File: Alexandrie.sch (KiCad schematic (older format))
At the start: 61 parts

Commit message: Angelia lpf/hpf Control board
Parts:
- removed U?: TPIC6B595, symbol TPIC6B595
- removed U?: 74HCT04, symbol 74HCT04
- added C11, C13, C15, C16, C18, C20: 100n, symbol C_Small
- added C12, C14, C17, C19: 10u, symbol CP_Small
- added J5: CONN_01X02, symbol CONN_01X02
- added U11: LD29150DT50R, symbol 7805D-Pack
- added U12: L4940D2T12, symbol 7805D-Pack
- added unit 2 of U2
- added U8: TPIC6B595, symbol TPIC6B595-RESCUE-Alexandrie-RESCUE-Alexandrie
- J1: renamed from J?; value CONN_01X10 -> kk_10
- J2: renamed from J?; value CONN_01X05 -> kk_5
- J3: renamed from J?; value Antenna_Conn -> kk_5
- J4: renamed from J?; value CONN_01X02 -> kk_2
- J6: renamed from J?; value To LPF_1 board -> kk_10
- J7: renamed from J?; value To LPF_2 board -> kk_10
- J8: renamed from J?; value To RX1 Filter Board -> kk_10
- J9: renamed from J?; value To RX2 Filter Board -> kk_10
- U10, U3, U4, U5, U6, U7, U9: renamed from U?; symbol TPIC6B595 -> TPIC6B595-RESCUE-Alexandrie-RESCUE-Alexandrie
- gave numbers to parts that had none: 35
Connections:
- net labels removed: FWD_PWR, REFL_PWR, SPI_TX_Load, TXRX_Status
- wire segments 311 -> 330
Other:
- note added: "12V"
- note added: "12V\n"
- note added: "5V"
- note added: "Antenna Cont."
- note added: "FWD_PWR\n"
- note added: "REFL_PWR"
- note added: "TXRX_Status"
- note added: "To Arduino\nControl Board"
- note added: "To LPF_1 board"
- note added: "To LPF_2 board\n"
- note added: "To RX1 HPF1 Board"
- note added: "To RX2 HPF2 Board"
- note added: "To coupler\nT/R board"

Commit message: final schematic drawing
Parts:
- removed J4: kk_2, symbol CONN_01X02
- added J10: CONN_01X02, symbol CONN_01X02
- added J4: CONN_01X06, symbol CONN_01X06
- U10, U3, U4, U5, U6, U7, U8, U9: symbol TPIC6B595-RESCUE-Alexandrie-RESCUE-Alexandrie -> TPIC6B595-RESCUE-Alexandrie-RESCUE-Alexandrie-RESCUE-Alexandrie
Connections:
- wire segments 330 -> 335
- no-connect marks 27 -> 26
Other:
- note added: "-->\nTX/RX\nRelay"
- note added: "<--\nFWD"
- note added: "<--\nRefl"
- note added: "Secondary TX/RX \nRelay cmd"
- note added: "To Mentor\nCtrl Brd\n\n\n"
- note added: "To\nVSWR/PS/TX-RX \nBoard"
- note removed: "???"
- note removed: "To Arduino\nControl Board"
- note removed: "To coupler\nT/R board"
- moved on the sheet: J2, R7

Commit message: minor schematic errors fixed
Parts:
- removed U10, U3, U4, U5, U6, U7, U8, U9: TPIC6B595, symbol TPIC6B595-RESCUE-Alexandrie-RESCUE-Alexandrie-RESCUE-Alexandrie
- added U10, U3, U4, U5, U6, U7, U8, U9: TPIC6B595, Housings_SOIC:SOIC-20W_7.5x12.8mm_Pitch1.27mm, symbol TPIC6B595
- C1, C10, C11, C13, C15, C16, C18, C2, C20, C3, C4, C5, C6, C7, C8, C9: footprint (none) -> Capacitors_SMD:C_0805_HandSoldering
- J1, J6, J7, J8, J9: footprint (none) -> conn_kk100:kk100_22-23-2101
- J10, J5: footprint (none) -> conn_kk100:kk100_22-23-2021
- J2, J3: footprint (none) -> conn_kk100:kk100_22-23-2051
- J4: footprint (none) -> conn_kk100:kk100_22-23-2061
- R1, R10, R11, R12, R13, R14, R15, R2, R3, R4, R5, R6, R7, R8, R9: footprint (none) -> Resistors_SMD:R_0805_HandSoldering
- U1, U2: footprint (none) -> Housings_SOIC:SOIC-14_3.9x8.7mm_Pitch1.27mm
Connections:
- no-connect marks 26 -> 42

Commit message: Alexandrie V 1.0 pcb routing w/o power supply
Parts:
- added TP1, TP2: TEST, Mounting_Holes:MountingHole_3.5mm_Pad, symbol TEST
- C12, C14, C17, C19: footprint (none) -> Capacitors_Tantalum_SMD:CP_Tantalum_Case-C_EIA-6032-28_Hand
- D1, D2, D3, D4, D5, D6, D7, D8: footprint (none) -> smd_leds:Led_1206
- U11, U12: footprint (none) -> TO_SOT_Packages_SMD:TO-263-3_TabPin4
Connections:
- net GND: now also TP1.1, TP2.1
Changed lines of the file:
@@
 F 0 "D2" H 5200 6450 50  0000 C CNN
 F 1 "LED" H 5200 6250 50  0000 C CNN
-F 2 "" H 5200 6350 50  0001 C CNN
+F 2 "smd_leds:Led_1206" H 5200 6350 50  0001 C CNN
 F 3 "" H 5200 6350 50  0001 C CNN
 	1    5200 6350
@@
 F 0 "D6" H 6450 7150 50  0000 C CNN
 F 1 "LED" H 6450 6950 50  0000 C CNN
-F 2 "" H 6450 7050 50  0001 C CNN
+F 2 "smd_leds:Led_1206" H 6450 7050 50  0001 C CNN
 F 3 "" H 6450 7050 50  0001 C CNN
 	1    6450 7050
@@
 F 0 "D1" H 5200 4650 50  0000 C CNN
 F 1 "LED" H 5200 4450 50  0000 C CNN
-F 2 "" H 5200 4550 50  0001 C CNN
+F 2 "smd_leds:Led_1206" H 5200 4550 50  0001 C CNN
 F 3 "" H 5200 4550 50  0001 C CNN
 	1    5200 4550
@@
 F 0 "D5" H 6450 5350 50  0000 C CNN
 F 1 "LED" H 6450 5150 50  0000 C CNN
-F 2 "" H 6450 5250 50  0001 C CNN
+F 2 "smd_leds:Led_1206" H 6450 5250 50  0001 C CNN
 F 3 "" H 6450 5250 50  0001 C CNN
 	1    6450 5250
@@
 F 0 "D4" H 5600 3000 50  0000 C CNN
 F 1 "LED" H 5600 2800 50  0000 C CNN
-F 2 "" H 5600 2900 50  0001 C CNN
+F 2 "smd_leds:Led_1206" H 5600 2900 50  0001 C CNN
 F 3 "" H 5600 2900 50  0001 C CNN
 	1    5600 2900
@@
 F 0 "D8" H 7900 3000 50  0000 C CNN
 F 1 "LED" H 7900 2800 50  0000 C CNN
-F 2 "" H 7900 2900 50  0001 C CNN
+F 2 "smd_leds:Led_1206" H 7900 2900 50  0001 C CNN
 F 3 "" H 7900 2900 50  0001 C CNN
 	1    7900 2900
@@
 F 0 "D3" H 5600 1350 50  0000 C CNN
 F 1 "LED" H 5600 1150 50  0000 C CNN
-F 2 "" H 5600 1250 50  0001 C CNN
+F 2 "smd_leds:Led_1206" H 5600 1250 50  0001 C CNN
 F 3 "" H 5600 1250 50  0001 C CNN
 	1    5600 1250
@@
 F 0 "D7" H 7900 1350 50  0000 C CNN
 F 1 "LED" H 7900 1150 50  0000 C CNN
-F 2 "" H 7900 1250 50  0001 C CNN
+F 2 "smd_leds:Led_1206" H 7900 1250 50  0001 C CNN
 F 3 "" H 7900 1250 50  0001 C CNN
 	1    7900 1250
@@
 F 0 "U11" H 8200 4904 50  0000 C CNN
 F 1 "LD29150DT50R" H 7700 5300 50  0000 C CNN
-F 2 "" H 8050 5100 50  0001 C CNN
+F 2 "TO_SOT_Packages_SMD:TO-263-3_TabPin4" H 8050 5100 50  0001 C CNN
 F 3 "" H 8050 5100 50  0001 C CNN
 	1    8050 5100
@@
 F 0 "C14" H 8110 5770 50  0000 L CNN
 F 1 "10u" V 8000 5650 50  0000 L CNN
-F 2 "" H 8100 5700 50  0001 C CNN
+F 2 "Capacitors_Tantalum_SMD:CP_Tantalum_Case-C_EIA-6032-28_Hand" H 8100 5700 50  0001 C CNN
 F 3 "" H 8100 5700 50  0001 C CNN
 	1    8100 5700
@@
 F 0 "C12" H 8110 4720 50  0000 L CNN
 F 1 "10u" V 8000 4600 50  0000 L CNN
-F 2 "" H 8100 4650 50  0001 C CNN
+F 2 "Capacitors_Tantalum_SMD:CP_Tantalum_Case-C_EIA-6032-28_Hand" H 8100 4650 50  0001 C CNN
 F 3 "" H 8100 4650 50  0001 C CNN
 	1    8100 4650
@@
 F 0 "U12" H 9300 4904 50  0000 C CNN
 F 1 "L4940D2T12" H 8850 5300 50  0000 C CNN
-F 2 "" H 9150 5100 50  0001 C CNN
+F 2 "TO_SOT_Packages_SMD:TO-263-3_TabPin4" H 9150 5100 50  0001 C CNN
 F 3 "" H 9150 5100 50  0001 C CNN
 	1    9150 5100
@@
 F 0 "C19" H 9210 5770 50  0000 L CNN
 F 1 "10u" V 9100 5650 50  0000 L CNN
-F 2 "" H 9200 5700 50  0001 C CNN
+F 2 "Capacitors_Tantalum_SMD:CP_Tantalum_Case-C_EIA-6032-28_Hand" H 9200 5700 50  0001 C CNN
 F 3 "" H 9200 5700 50  0001 C CNN
 	1    9200 5700
@@
 F 0 "C17" H 9210 4720 50  0000 L CNN
 F 1 "10u" V 9100 4600 50  0000 L CNN
-F 2 "" H 9200 4650 50  0001 C CNN
+F 2 "Capacitors_Tantalum_SMD:CP_Tantalum_Case-C_EIA-6032-28_Hand" H 9200 4650 50  0001 C CNN
 F 3 "" H 9200 4650 50  0001 C CNN
 	1    9200 4650
@@
 NoConn ~ 5000 850
 NoConn ~ 4500 850
+$Comp
+L TEST TP1
+U 1 1 592BBEFC
+P 8550 900
+F 0 "TP1" H 8550 1200 50  0000 C BNN
+F 1 "TEST" H 8550 1150 50  0000 C CNN
+F 2 "Mounting_Holes:MountingHole_3.5mm_Pad" H 8550 900 50  0001 C CNN
+F 3 "" H 8550 900 50  0001 C CNN
+	1    8550 900
+	1    0    0    -1
+$EndComp
+$Comp
+L TEST TP2
+U 1 1 592BBFC7
+P 8850 900
+F 0 "TP2" H 8850 1200 50  0000 C BNN
+F 1 "TEST" H 8850 1150 50  0000 C CNN
+F 2 "Mounting_Holes:MountingHole_3.5mm_Pad" H 8850 900 50  0001 C CNN
+F 3 "" H 8850 900 50  0001 C CNN
+	1    8850 900
+	1    0    0    -1
+$EndComp
+$Comp
+L GND #PWR087
+U 1 1 592BC282
+P 8850 950
+F 0 "#PWR087" H 8850 700 50  0001 C CNN
+F 1 "GND" H 8850 800 50  0000 C CNN
+F 2 "" H 8850 950 50  0001 C CNN
+F 3 "" H 8850 950 50  0001 C CNN
+	1    8850 950
+	1    0    0    -1
+$EndComp
+Wire Wire Line
+	8850 900  8850 950
+$Comp
+L GND #PWR088
+U 1 1 592BC2D8
+P 8550 950
+F 0 "#PWR088" H 8550 700 50  0001 C CNN
+F 1 "GND" H 8550 800 50  0000 C CNN
+F 2 "" H 8550 950 50  0001 C CNN
+F 3 "" H 8550 950 50  0001 C CNN
+	1    8550 950
+	1    0    0    -1
+$EndComp
+Wire Wire Line
+	8550 900  8550 950
 $EndSCHEMATC

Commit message: final beta, Sylkmask to annotate
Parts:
- U12: value L4940D2T12 -> LD29150DT50R
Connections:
- net +12V: now also C13.2, C14.2, C15.2, C16.2, C17.2, U11.1 (In), U12.1 (In)
- net +5V: now also C11.2, C12.2, U11.3 (Out)
- net at C18.2, C19.2, C20.2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: now also U12.3 (Out); no longer U12.1 (In)
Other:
- note removed: "5V"
- moved on the sheet: C11, C12, C13, C14, C15

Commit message: RTM with sylkmask
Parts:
- added D9: D, Diodes_SMD:D_SMB_Handsoldering, symbol D
- added J11: CONN_01X03, conn_kk100:kk100_22-23-2031, symbol CONN_01X03
- added TP3, TP4: TEST, Mounting_Holes:MountingHole_3.5mm_Pad, symbol TEST
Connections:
- net +12V: now also D9.1 (K)
- net GND: now also J11.3 (P3), TP3.1, TP4.1
- new net: D9.2 (A), J11.1 (P1), J11.2 (P2)
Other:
- note added: "12V In"
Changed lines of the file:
@@
 	0    -1   1    0
 $EndComp
+$Comp
+L TEST TP3
+U 1 1 592E5FB7
+P 9550 900
+F 0 "TP3" H 9550 1200 50  0000 C BNN
+F 1 "TEST" H 9550 1150 50  0000 C CNN
+F 2 "Mounting_Holes:MountingHole_3.5mm_Pad" H 9550 900 50  0001 C CNN
+F 3 "" H 9550 900 50  0001 C CNN
+	1    9550 900
+	1    0    0    -1
+$EndComp
+$Comp
+L TEST TP4
+U 1 1 592E5FBD
+P 9850 900
+F 0 "TP4" H 9850 1200 50  0000 C BNN
+F 1 "TEST" H 9850 1150 50  0000 C CNN
+F 2 "Mounting_Holes:MountingHole_3.5mm_Pad" H 9850 900 50  0001 C CNN
+F 3 "" H 9850 900 50  0001 C CNN
+	1    9850 900
+	1    0    0    -1
+$EndComp
+$Comp
+L GND #PWR087
+U 1 1 592E5FC3
+P 9850 950
+F 0 "#PWR087" H 9850 700 50  0001 C CNN
+F 1 "GND" H 9850 800 50  0000 C CNN
+F 2 "" H 9850 950 50  0001 C CNN
+F 3 "" H 9850 950 50  0001 C CNN
+	1    9850 950
+	1    0    0    -1
+$EndComp
+$Comp
+L GND #PWR088
+U 1 1 592E5FC9
+P 9550 950
+F 0 "#PWR088" H 9550 700 50  0001 C CNN
+F 1 "GND" H 9550 800 50  0000 C CNN
+F 2 "" H 9550 950 50  0001 C CNN
+F 3 "" H 9550 950 50  0001 C CNN
+	1    9550 950
+	1    0    0    -1
+$EndComp
+Wire Wire Line
+	9850 900  9850 950
+Wire Wire Line
+	9550 900  9550 950
+$Comp
+L CONN_01X03 J11
+U 1 1 592EBACE
+P 9500 3750
+F 0 "J11" H 9500 3950 50  0000 C CNN
+F 1 "CONN_01X03" V 9600 3750 50  0000 C CNN
+F 2 "conn_kk100:kk100_22-23-2031" H 9500 3750 50  0001 C CNN
+F 3 "" H 9500 3750 50  0001 C CNN
+	1    9500 3750
+	1    0    0    -1
+$EndComp
+$Comp
+L +12V #PWR089
+U 1 1 592EC4AF
+P 8950 3700
+F 0 "#PWR089" H 8950 3550 50  0001 C CNN
+F 1 "+12V" H 8950 3840 50  0000 C CNN
+F 2 "" H 8950 3700 50  0001 C CNN
+F 3 "" H 8950 3700 50  0001 C CNN
+	1    8950 3700
+	0    -1   -1   0
+$EndComp
+$Comp
+L GND #PWR090
+U 1 1 592EC505
+P 9250 3850
+F 0 "#PWR090" H 9250 3600 50  0001 C CNN
+F 1 "GND" V 9250 3650 50  0000 C CNN
+F 2 "" H 9250 3850 50  0001 C CNN
+F 3 "" H 9250 3850 50  0001 C CNN
+	1    9250 3850
+	0    1    1    0
+$EndComp
+Wire Wire Line
+	9300 3850 9250 3850
+$Comp
+L D D9
+U 1 1 592ECDDA
+P 9150 3700
+F 0 "D9" H 9150 3800 50  0000 C CNN
+F 1 "D" H 9150 3600 50  0000 C CNN
+F 2 "Diodes_SMD:D_SMB_Handsoldering" H 9150 3700 50  0001 C CNN
+F 3 "" H 9150 3700 50  0001 C CNN
+	1    9150 3700
+	1    0    0    -1
+$EndComp
+Wire Wire Line
+	9300 3650 9300 3750
+Connection ~ 9300 3700
+Text Notes 9750 3900 1    60   ~ 0
+12V In
+Wire Wire Line
+	9000 3700 8950 3700
 $EndSCHEMATC

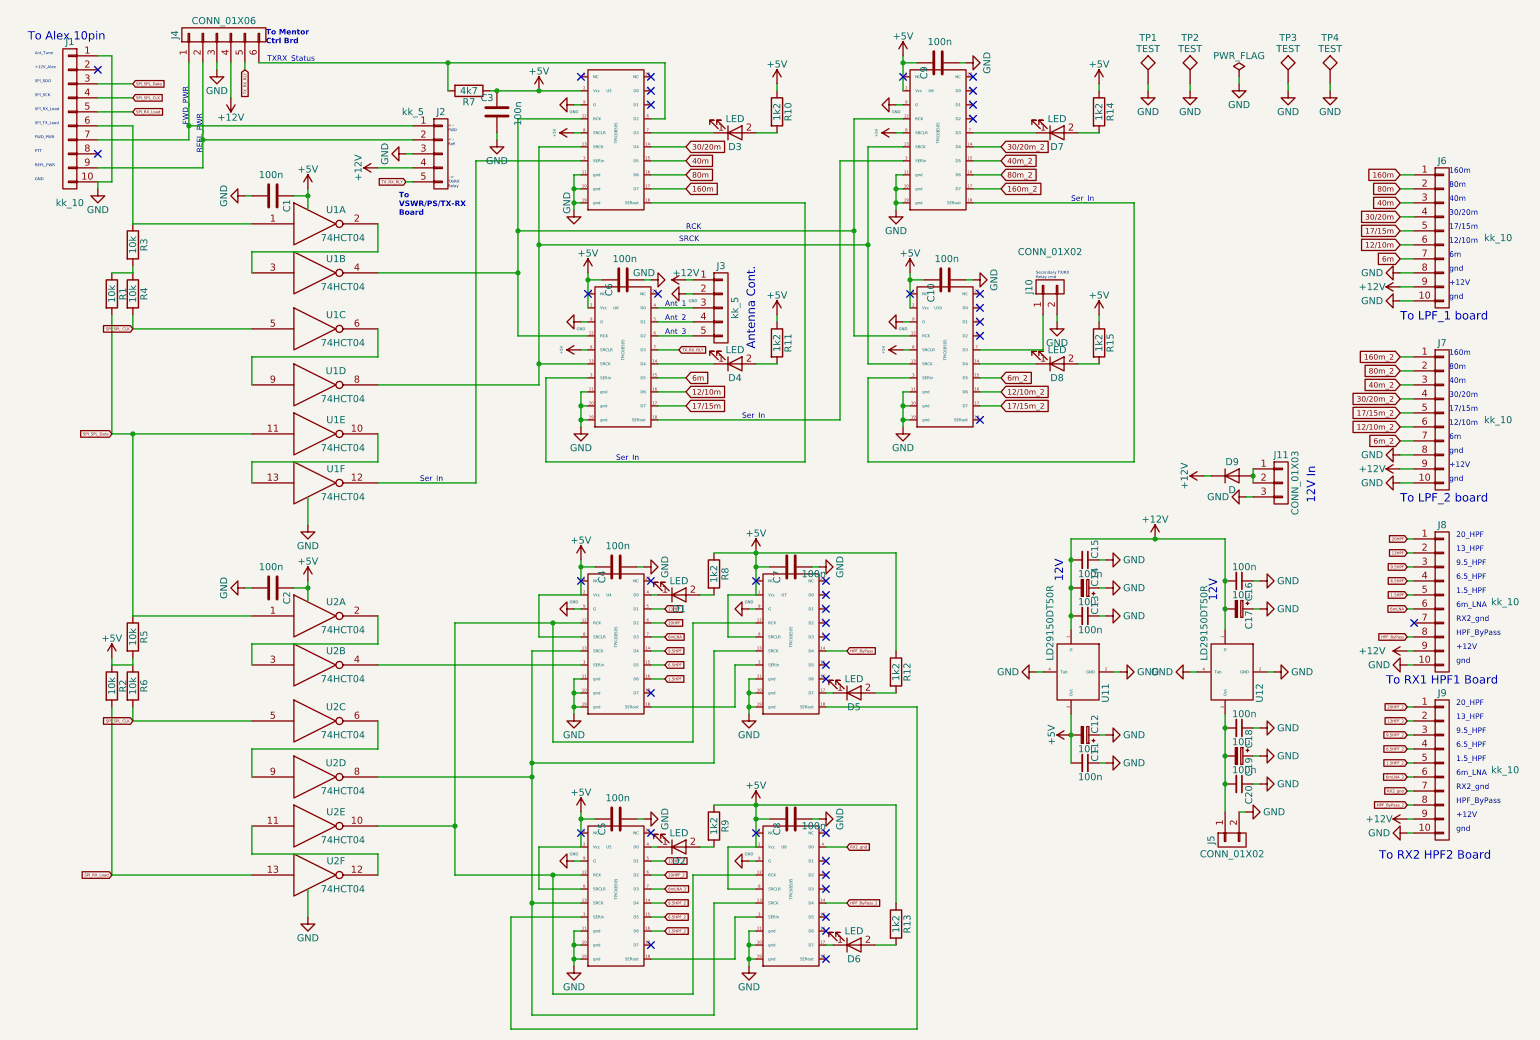
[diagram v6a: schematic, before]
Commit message: Complete redrawing, Alexiares compatible
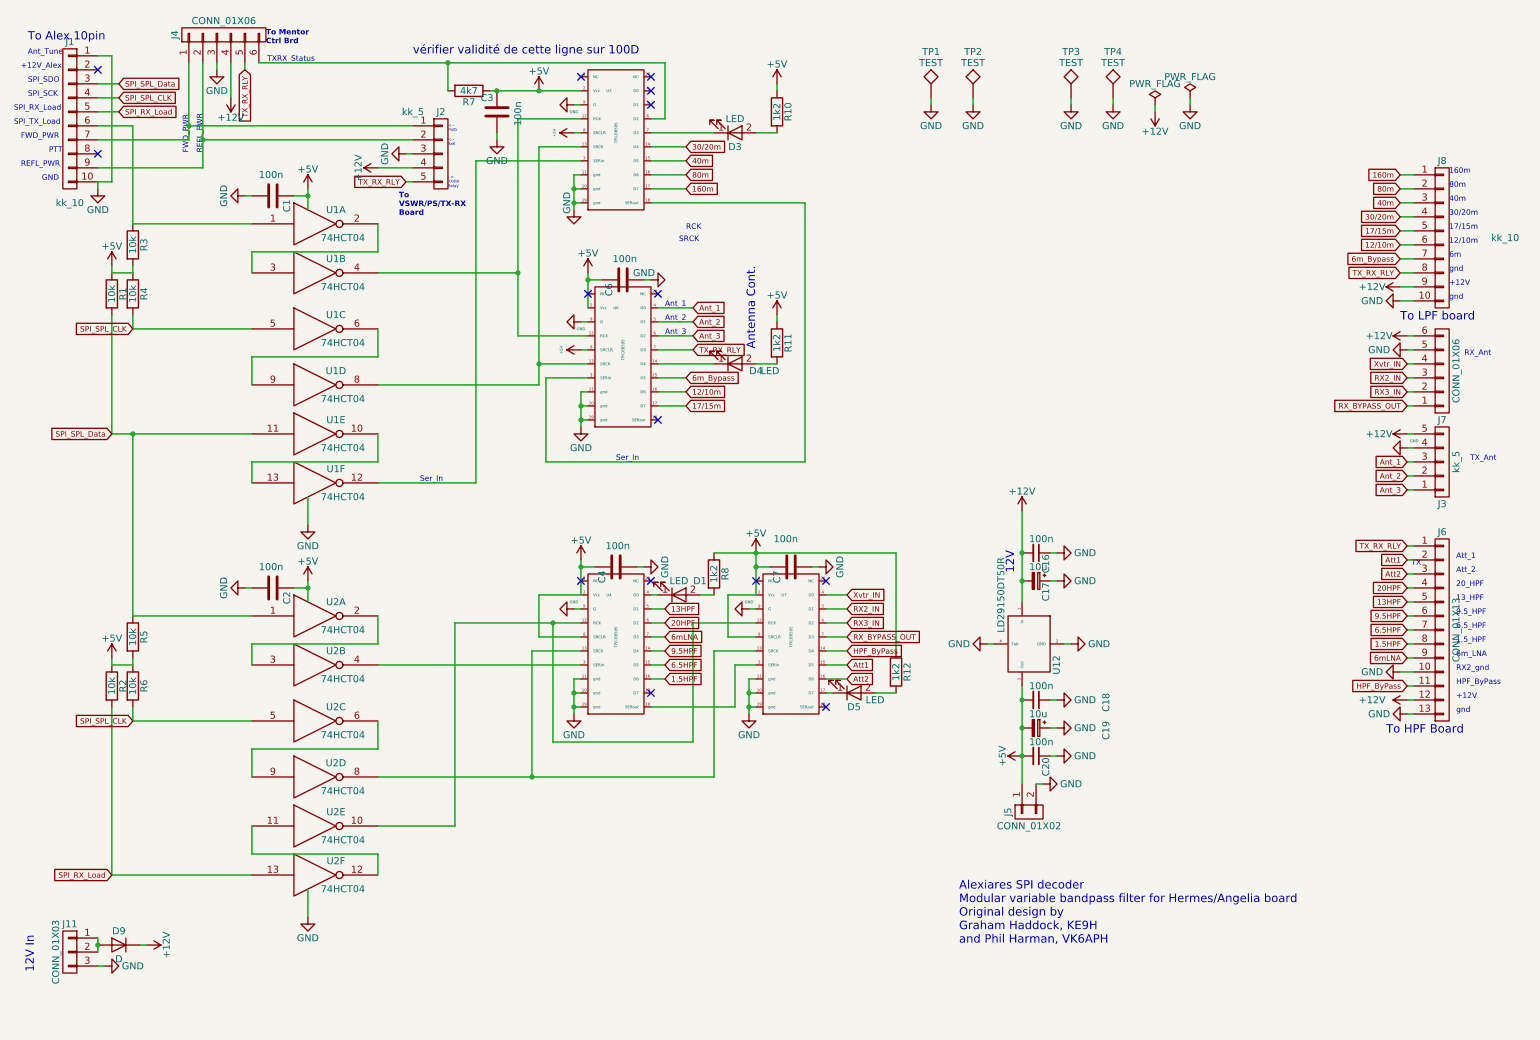
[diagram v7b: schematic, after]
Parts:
- removed C10, C5, C8, C9: 100n, Capacitors_SMD:C_0805_HandSoldering, symbol C
- removed C11, C13, C15: 100n, Capacitors_SMD:C_0805_HandSoldering, symbol C_Small
- removed C12, C14: 10u, Capacitors_Tantalum_SMD:CP_Tantalum_Case-C_EIA-6032-28_Hand, symbol CP_Small
- removed D2, D6, D7, D8: LED, smd_leds:Led_1206, symbol LED
- removed J10: CONN_01X02, conn_kk100:kk100_22-23-2021, symbol CONN_01X02
- removed J6, J7, J9: kk_10, conn_kk100:kk100_22-23-2101, symbol CONN_01X10
- removed R13, R14, R15, R9: 1k2, Resistors_SMD:R_0805_HandSoldering, symbol R
- removed U10, U5, U8, U9: TPIC6B595, Housings_SOIC:SOIC-20W_7.5x12.8mm_Pitch1.27mm, symbol TPIC6B595
- removed U11: LD29150DT50R, TO_SOT_Packages_SMD:TO-263-3_TabPin4, symbol 7805D-Pack
- added J6: CONN_01X13, conn_kk100:kk100_22-23-2131, symbol CONN_01X13
- added J7: CONN_01X06, conn_kk100:kk100_22-23-2061, symbol CONN_01X06
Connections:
- net 6m is gone; now on net 6m_Bypass: U6.15 (D5)
- net +12V: now also J3.5 (P5), J6.12 (P12), J7.6 (P6); no longer J3.1 (P1)
- net +5V: now also C18.2, C19.2, C20.2, J5.1 (P1), R1.1, R3.2, R4.1, U12.3 (Out)
- net 1.5HPF: now also J6.8 (P8); no longer J8.5 (P5)
- net 12/10m: now also J8.6 (P6)
- net 13HPF: now also J6.5 (P5); no longer J8.2 (P2)
- net 160m: now also J8.1 (P1)
- net 17/15m: now also J8.5 (P5)
- net 20HPF: now also J6.4 (P4); no longer J8.1 (P1)
- net 30/20m: now also J8.4 (P4)
- net 40m: now also J8.3 (P3)
- net 6.5HPF: now also J6.7 (P7); no longer J8.4 (P4)
- net 6mLNA: now also J6.9 (P9); no longer J8.6 (P6)
- net 80m: now also J8.2 (P2)
- net 9.5HPF: now also J6.6 (P6); no longer J8.3 (P3)
- net GND: now also J3.4 (P4), J6.10 (P10), J6.13 (P13), J7.5 (P5); no longer J3.2 (P2)
- net HPF_ByPass: now also J6.11 (P11); no longer J8.8 (P8)
- net TX_RX_RLY: now also J8.8 (P8), J6.1 (P1)
- net Ant_1: now reaches J3.3 (P3), U6.4 (D0)
- net Ant_2: now reaches U6.5 (D1)
- net Ant_2: now also J3.2 (P2); no longer J3.4 (P4)
- net Ant_3: now reaches U6.6 (D2)
- net Ant_3: now also J3.1 (P1); no longer J3.5 (P5)
- net 6m_Bypass: now reaches J8.7 (P7)
- net Att1: now reaches U7.15 (D5)
- net Att1: now also J6.2 (P2)
- net Att2: now reaches U7.16 (D6)
- net Att2: now also J6.3 (P3)
- net Xvtr_IN: now reaches U7.4 (D0)
- net Xvtr_IN: now also J7.4 (P4)
- net RX2_IN: now reaches U7.5 (D1)
- net RX2_IN: now also J7.3 (P3)
- net RX3_IN: now reaches U7.6 (D2)
- net RX3_IN: now also J7.2 (P2)
- net RX_BYPASS_OUT: now reaches U7.7 (D3)
- net RX_BYPASS_OUT: now also J7.1 (P1)
- no-connect marks 42 -> 15
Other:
- note added: "Alexiares SPI decoder\nModular variable bandpass filter for Hermes/Angelia board\nOriginal design by \nGraham Haddock, KE9H\nand Phil Harman, VK6APH"
- note added: "Att_1\n"
- note added: "Att_2"
- note added: "RX_Ant\n"
- note added: "TX"
- note added: "TX_Ant"
- note added: "To HPF Board"
- note added: "To LPF board"
- note added: "vérifier validité de cette ligne sur 100D\n"
- note removed: "12V"
- note removed: "Secondary TX/RX \nRelay cmd"
- note removed: "To LPF_1 board"
- note removed: "To LPF_2 board\n"
- note removed: "To RX1 HPF1 Board"
- note removed: "To RX2 HPF2 Board"
- moved on the sheet: C16, C17, C18, C19, C20, D9, J11, J5, J8, TP1, TP2, TP3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

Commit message: new footprint for drivers
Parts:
- U3, U4, U6, U7: footprint Housings_SOIC:SOIC-20W_7.5x12.8mm_Pitch1.27mm -> Housings_SOIC:SO-20_12.8x7.5mm_Pitch1.27mm
